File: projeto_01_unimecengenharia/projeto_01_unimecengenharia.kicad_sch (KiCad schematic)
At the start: 2 parts

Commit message: mais alguns ajustes
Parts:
- added R2: R_US, symbol Device:R_US
- added R3: 4k7, symbol Device:R_US
- added U1: ATmega328-A, Package_QFP:TQFP-32_7x7mm_P0.8mm, symbol MCU_Microchip_ATmega:ATmega328-A
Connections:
- new net: U1.21 (GND), U1.3 (GND), U1.5 (GND)
- new net: U1.7 (XTAL1/PB6), U1.8 (XTAL2/PB7)
- new net VCC: U1.18 (AVCC), U1.4 (VCC), U1.6 (VCC)

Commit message: Apaguei tudo
Vamos começar a projetar de verdade
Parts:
- removed D1: LED, symbol Device:LED
- removed R1: R, symbol Device:R
- removed R2: R_US, symbol Device:R_US
- removed R3: 4k7, symbol Device:R_US
- removed U1: ATmega328-A, Package_QFP:TQFP-32_7x7mm_P0.8mm, symbol MCU_Microchip_ATmega:ATmega328-A

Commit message: coloquei o esp32 e o modulo
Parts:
- added U1: ESP32-WROOM-32D, RF_Module:ESP32-WROOM-32D, symbol RF_Module:ESP32-WROOM-32D
- added U2: SIM7080G, SIM7080G:XCVR_SIM7080G, symbol SIM7080G:SIM7080G
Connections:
- new net: U1.1 (GND), U1.15 (GND), U1.38 (GND), U1.39 (GND)
- new net GND: U2.13 (GND), U2.19 (GND), U2.21 (GND), U2.27 (GND), U2.30 (GND), U2.31 (GND), U2.33 (GND), U2.36 (GND), U2.37 (GND), U2.45 (GND), U2.63 (GND), U2.66 (GND), U2.67 (GND), U2.69 (GND), U2.70 (GND), U2.71 (GND), U2.72 (GND), U2.73 (GND), U2.74 (GND), U2.75 (GND), U2.76 (GND), U2.77 (GND), U2.8 (GND)
- new net VBAT: U2.34 (VBAT), U2.35 (VBAT)

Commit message: coloquei mais componentes
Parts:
- added U3: ADS1115IDGS, Package_SO:TSSOP-10_3x3mm_P0.5mm, symbol Analog_ADC:ADS1115IDGS
- added U4: DS3231MZ, Package_SO:SOIC-8_3.9x4.9mm_P1.27mm, symbol Timer_RTC:DS3231MZ
- added U5: MAX3485, Package_SO:SOIC-8_3.9x4.9mm_P1.27mm, symbol Interface_UART:MAX3485
- added U6: LM2596S-ADJ, Package_TO_SOT_SMD:TO-263-5_TabPin3, symbol Regulator_Switching:LM2596S-ADJ

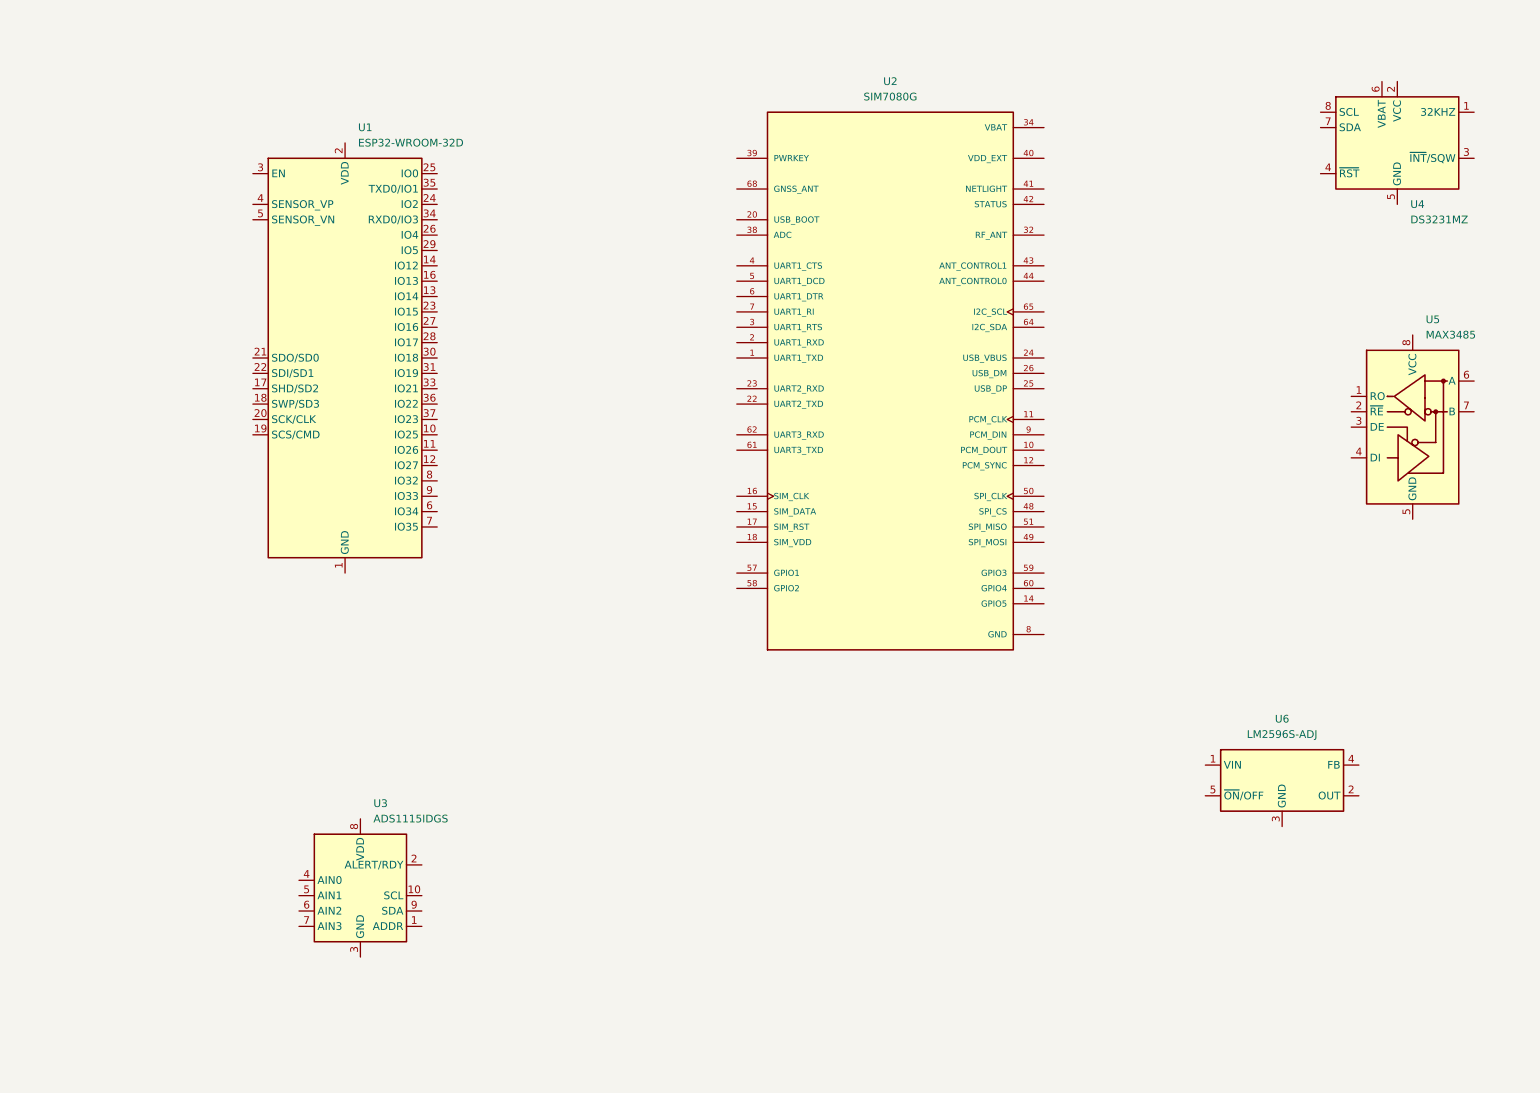
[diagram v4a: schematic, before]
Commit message: iniciei as ligações dos componentes
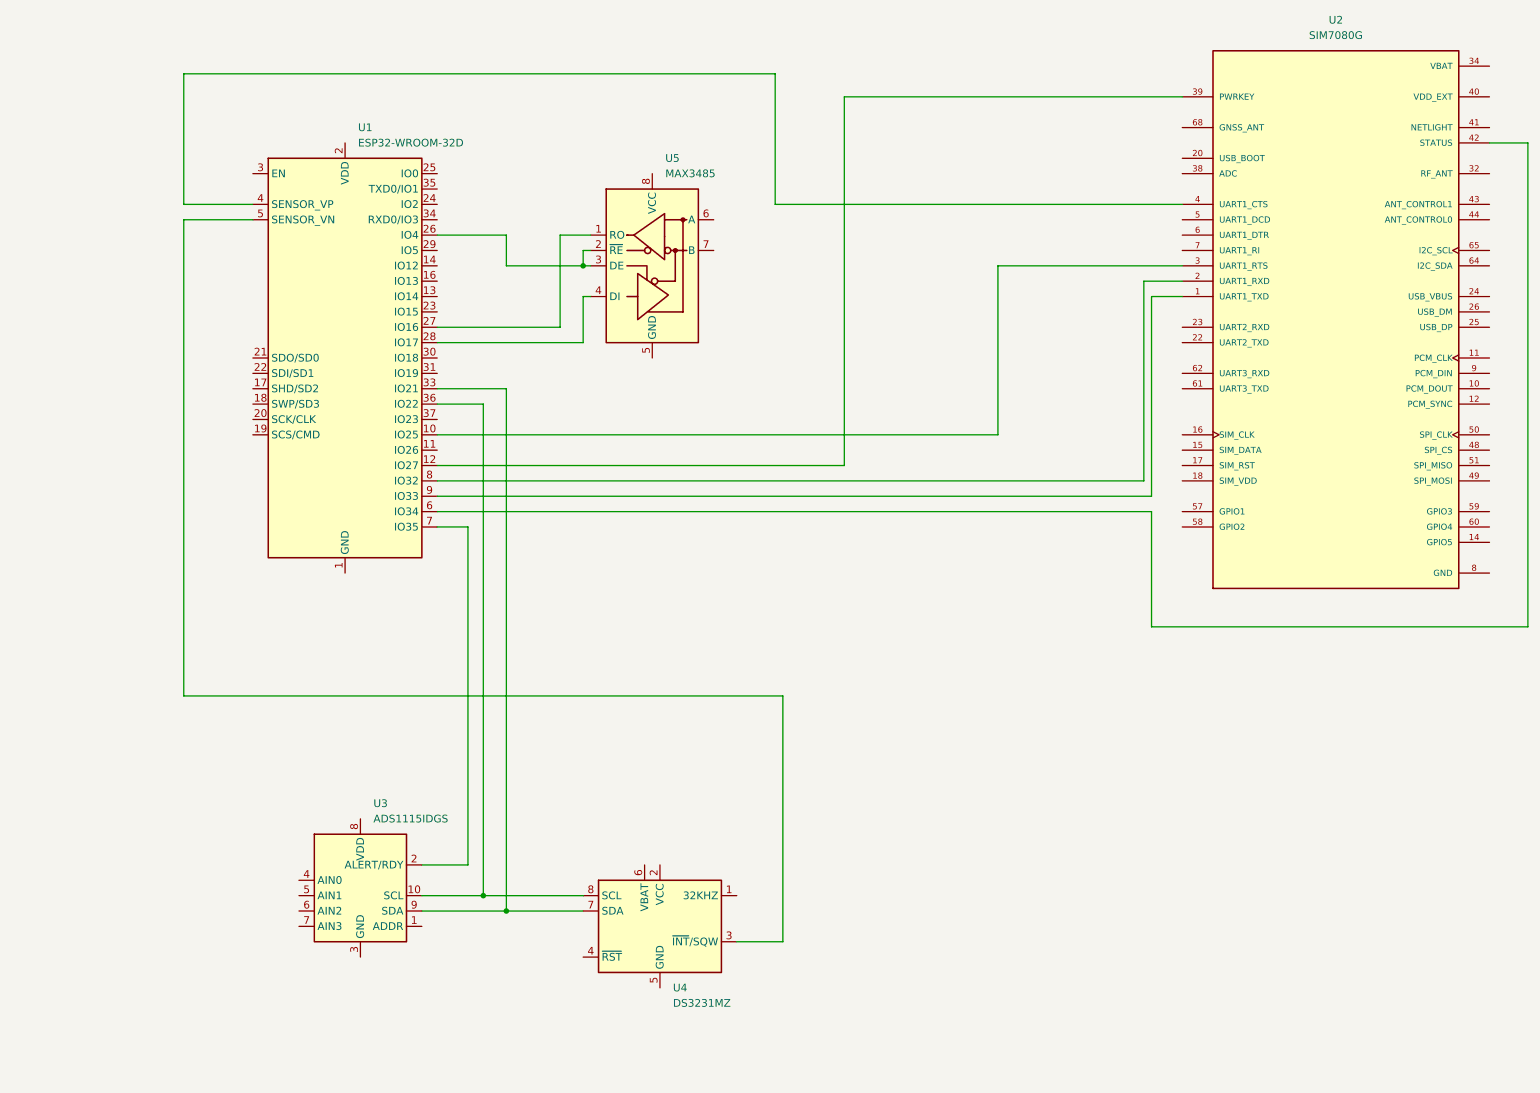
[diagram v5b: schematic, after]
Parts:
- removed U6: LM2596S-ADJ, Package_TO_SOT_SMD:TO-263-5_TabPin3, symbol Regulator_Switching:LM2596S-ADJ
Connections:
- net at U2.1 (UART1_TXD): now also U1.9 (IO33)
- net at U2.2 (UART1_RXD): now also U1.8 (IO32)
- net at U2.3 (UART1_RTS): now also U1.10 (IO25)
- net at U2.39 (PWRKEY): now also U1.12 (IO27)
- net at U2.4 (UART1_CTS): now also U1.4 (SENSOR_VP)
- net at U2.42 (STATUS): now also U1.6 (IO34)
- net at U1.26 (IO4): now also U5.2 (~{RE}), U5.3 (DE)
- net at U1.27 (IO16): now also U5.1 (RO)
- net at U1.28 (IO17): now also U5.4 (DI)
- net at U1.33 (IO21): now also U3.9 (SDA), U4.7 (SDA)
- net at U1.36 (IO22): now also U3.10 (SCL), U4.8 (SCL)
- net at U1.5 (SENSOR_VN): now also U4.3 (~{INT}/SQW)
- net at U1.7 (IO35): now also U3.2 (ALERT/RDY)
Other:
- moved on the sheet: U2, U4, U5

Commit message: fiz mais ligações
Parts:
- added R1, R2: 4,7k, symbol Device:R
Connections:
- net at U1.33 (IO21), U3.9 (SDA), U4.7 (SDA): now also R1.1
- net at U1.36 (IO22), U3.10 (SCL), U4.8 (SCL): now also R2.1
- new net VCC 3,3: R1.2, R2.2

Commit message: coloquei um ressitor
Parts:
- added R3: 10k, symbol Device:R
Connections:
- net VCC 3,3: now also R3.1
- net at U1.7 (IO35), U3.2 (ALERT/RDY): now also R3.2
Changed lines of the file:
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@@
+	)
+	(junction
+		(at 101.6 135.89)
+		(diameter 0)
+		(color 0 0 0 0)
 	)
 	(junction
@@
 	(wire
 		(pts
+			(xy 95.25 135.89) (xy 101.6 135.89)
+		)
+		(stroke
+			(width 0)
+			(type default)
+		)
+	)
+	(wire
+		(pts
 			(xy 153.67 124.46) (xy 54.61 124.46)
 		)
@@
 	(wire
 		(pts
+			(xy 101.6 135.89) (xy 101.6 152.4)
+		)
+		(stroke
+			(width 0)
+			(type default)
+		)
+	)
+	(wire
+		(pts
 			(xy 116.84 63.5) (xy 116.84 48.26)
 		)
@@
 	(wire
 		(pts
-			(xy 101.6 96.52) (xy 101.6 152.4)
+			(xy 101.6 96.52) (xy 101.6 135.89)
+		)
+		(stroke
+			(width 0)
+			(type default)
+		)
+	)
+	(wire
+		(pts
+			(xy 85.09 135.89) (xy 87.63 135.89)
 		)
 		(stroke
@@
 		(pts
 			(xy 107.95 53.34) (xy 107.95 48.26)
+		)
+		(stroke
+			(width 0)
+			(type default)
+		)
+	)
+	(wire
+		(pts
+			(xy 85.09 133.35) (xy 85.09 135.89)
 		)
 		(stroke
@@
 		(in_pos_files yes)
 		(dnp no)
-		(fields_autoplaced yes)
 		(property "Reference" "U2"
-			(at 245.11 12.7 0)
+			(at 245.11 13.97 0)
 			(show_name no)
 			(do_not_autoplace no)
@@
 		)
 		(property "Value" "SIM7080G"
-			(at 245.11 15.24 0)
+			(at 245.11 16.51 0)
 			(show_name no)
 			(do_not_autoplace no)
@@
 					(unit 1)
 				)
+			)
+		)
+	)
+	(symbol
+		(lib_id "Device:R")
+		(at 91.44 135.89 90)
+		(unit 1)
+		(body_style 1)
+		(exclude_from_sim no)
+		(in_bom yes)
+		(on_board yes)
+		(in_pos_files yes)
+		(dnp no)
+		(fields_autoplaced yes)
+		(property "Reference" "R3"
+			(at 91.44 129.54 90)
+			(show_name no)
+			(do_not_autoplace no)
+			(effects
+				(font
+					(size 1.27 1.27)
+				)
+			)
+		)
+		(property "Value" "10k"
+			(at 91.44 132.08 90)
+			(show_name no)
+			(do_not_autoplace no)
+			(effects
+				(font
+					(size 1.27 1.27)
+				)
+			)
+		)
+		(property "Footprint" ""
+			(at 91.44 137.668 90)
+			(hide yes)
+			(show_name no)
+			(do_not_autoplace no)
+			(effects
+				(font
+					(size 1.27 1.27)
+				)
+			)
+		)
+		(property "Datasheet" ""
+			(at 91.44 135.89 0)
+			(hide yes)
+			(show_name no)
+			(do_not_autoplace no)
+			(effects
+				(font
+					(size 1.27 1.27)
+				)
+			)
+		)
+		(property "Description" "Resistor"
+			(at 91.44 135.89 0)
+			(hide yes)
+			(show_name no)
+			(do_not_autoplace no)
+			(effects
+				(font
+					(size 1.27 1.27)
+				)
+			)
+		)
+		(pin "1"
+		)
+		(pin "2"
+		)
+		(instances
+			(project "projeto_01_unimecengenharia"
+				(path "/6d6de610-2d55-4130-a914-29a7528bf19d"
+					(reference "R3")
+					(unit 1)
+				)
+			)
+		)
+	)
+	(symbol
+		(lib_id "power:VCC")
+		(at 85.09 133.35 0)
+		(unit 1)
+		(body_style 1)
+		(exclude_from_sim no)
+		(in_bom yes)
+		(on_board yes)
+		(in_pos_files yes)
+		(dnp no)
+		(fields_autoplaced yes)
+		(property "Reference" "#PWR03"
+			(at 85.09 137.16 0)
+			(hide yes)
+			(show_name no)
+			(do_not_autoplace no)
+			(effects
+				(font
+					(size 1.27 1.27)
+				)
+			)
+		)
+		(property "Value" "VCC 3,3"
+			(at 85.09 128.27 0)
+			(show_name no)
+			(do_not_autoplace no)
+			(effects
+				(font
+					(size 1.27 1.27)
+				)
+			)
+		)
+		(property "Footprint" ""
+			(at 85.09 133.35 0)
+			(hide yes)
+			(show_name no)
+			(do_not_autoplace no)
+			(effects
+				(font
+					(size 1.27 1.27)
+				)
+			)
+		)
+		(property "Datasheet" ""
+			(at 85.09 133.35 0)
+			(hide yes)
+			(show_name no)
+			(do_not_autoplace no)
+			(effects
+				(font
+					(size 1.27 1.27)
+				)
+			)
+		)
+		(property "Description" "Power symbol creates a global label with name \"VCC\""
+			(at 85.09 133.35 0)
+			(hide yes)
+			(show_name no)
+			(do_not_autoplace no)
+			(effects
+				(font
+					(size 1.27 1.27)
+				)
+			)
+		)
+		(pin "1"
+		)
+		(instances
+			(project "projeto_01_unimecengenharia"
+				(path "/6d6de610-2d55-4130-a914-29a7528bf19d"
+					(reference "#PWR03")
+					(unit 1)
+				)
